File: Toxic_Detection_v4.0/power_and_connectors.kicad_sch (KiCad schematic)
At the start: 63 parts, among them IC7 ESDA6V1U1RL, IC8 AP7365-33WG-7, IC9 TPS2054BDR, J10 Conn_01x04_Pin, J11 USB_C_Receptacle, J12 DM3AT-SF-PEJM5, J13 Conn_01x04_Pin, J14 Conn_01x01_Pin, J15 Conn_01x01_Pin, J16 Conn_01x01_Pin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

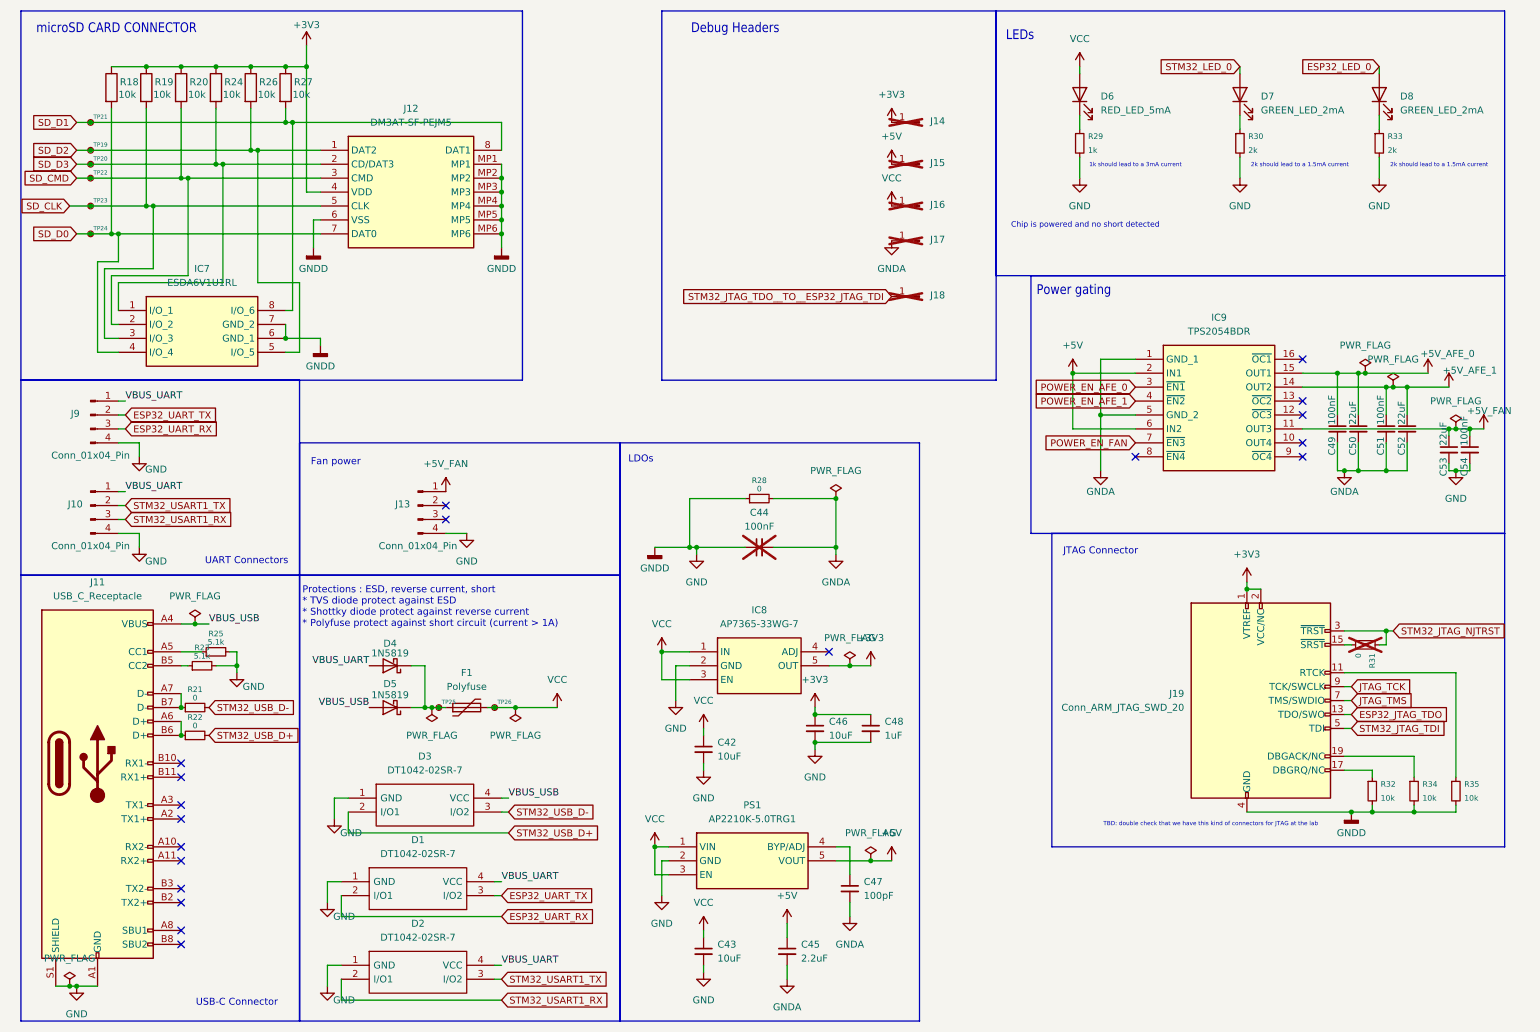
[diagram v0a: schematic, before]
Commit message: feat: first placement (layout)
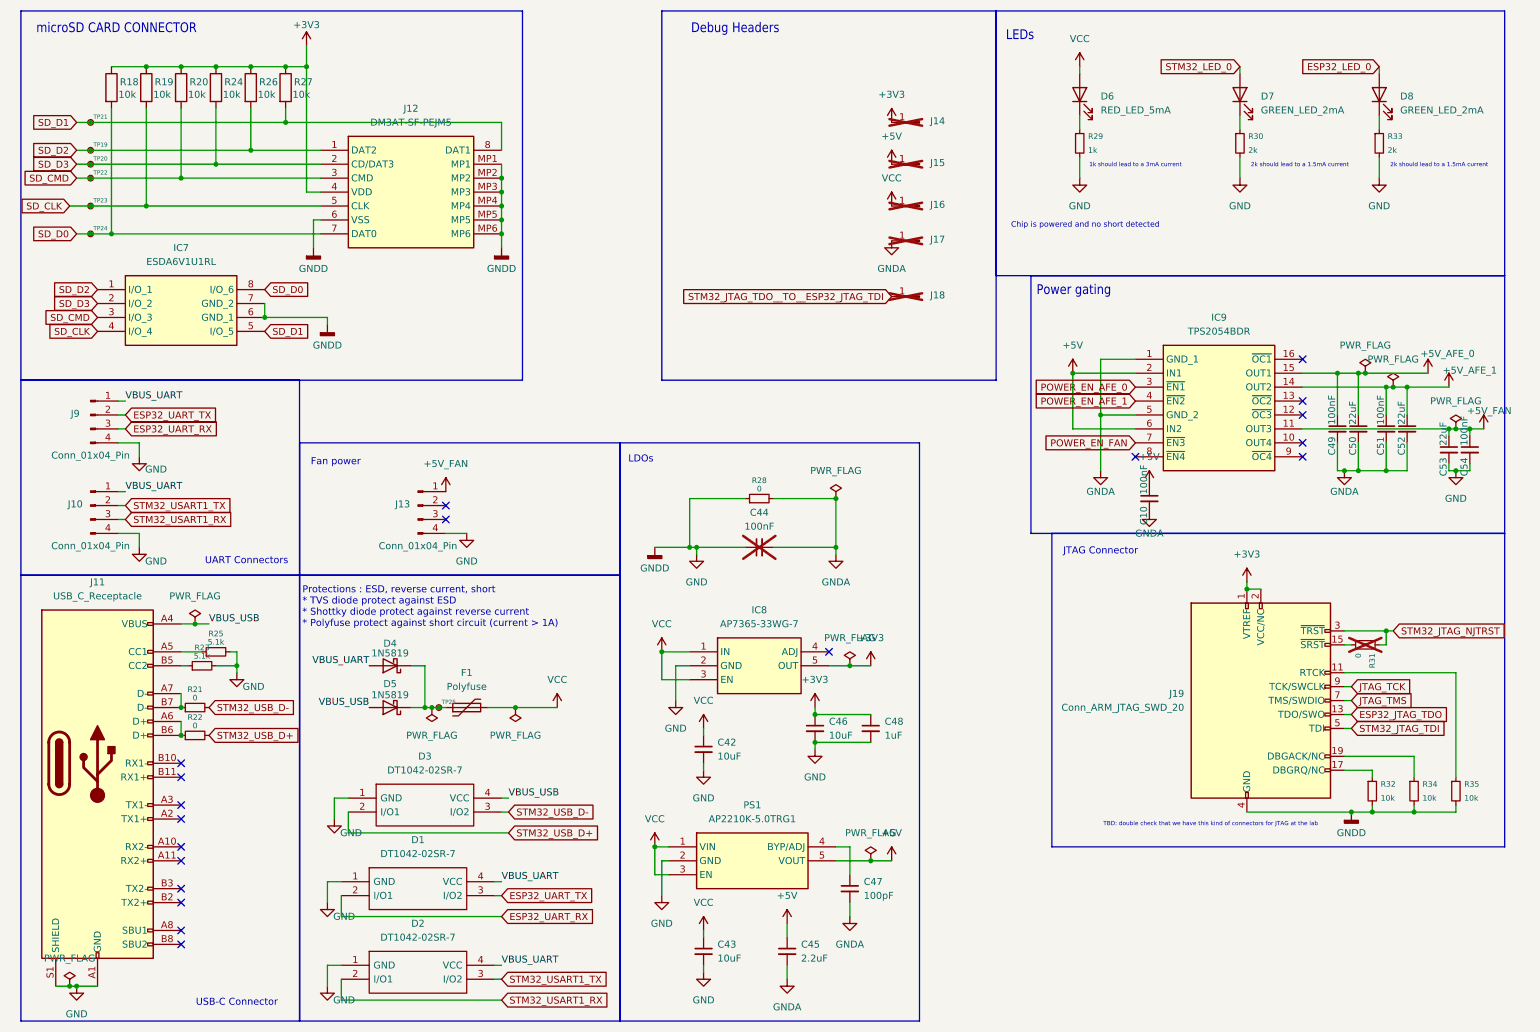
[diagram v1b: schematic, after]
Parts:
- removed TP26: TestPoint_Small, TestPoint:TestPoint_Pad_D1.0mm, symbol Connector:TestPoint_Small
- added C10: 100nF, Capacitor_SMD:C_0805_2012Metric_Pad1.18x1.45mm_HandSolder, symbol Device:C_Small
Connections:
- net +5V: now also C10.1
- net GNDA: now also C10.2
- net SD_CLK: now also IC7.4 (I/O_4); no longer IC7.3 (I/O_3)
- net SD_CMD: now also IC7.3 (I/O_3); no longer IC7.2 (I/O_2)
- net SD_D0: now also IC7.8 (I/O_6); no longer IC7.4 (I/O_4)
- net SD_D1: now also IC7.5 (I/O_5); no longer IC7.8 (I/O_6)
- net SD_D2: now also IC7.1 (I/O_1); no longer IC7.5 (I/O_5)
- net SD_D3: now also IC7.2 (I/O_2); no longer IC7.1 (I/O_1)
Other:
- moved on the sheet: IC7
